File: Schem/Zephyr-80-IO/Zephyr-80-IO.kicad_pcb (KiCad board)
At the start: 6 copper layers, 160 x 64.4 mm, 89 parts, among them IC1 Z80CTC, IC2 Z80SIO, IC3 Z80SIO, J1 pBITzBus, J2 548190519, J3 L77HDA26SD1CH4F, SW1 SW_Push, SW2 SW_Push, SW3 SW_Coded_SH-7070, SW4 SW_Coded_SH-7070, SW5 SW_Coded_SH-7070, SW6 SW_Coded_SH-7070, SW7 SW_Coded_SH-7030, SW8 SW_Coded_SH-7030, U1 ATmega1284-PU, U10 74HC688, U11 74HC688, U12 74HC688, U13 74HC244, U14 MAX202IDR, U2 74AHC1G125, U3 74AHC1G125, U4 74AHC595, U5 74AHC595, U6 74HC138, U7 FT230XS-U, U8 SN74HC4040DR, U9 74HC688, Y1 ECS-2100AX-147.4

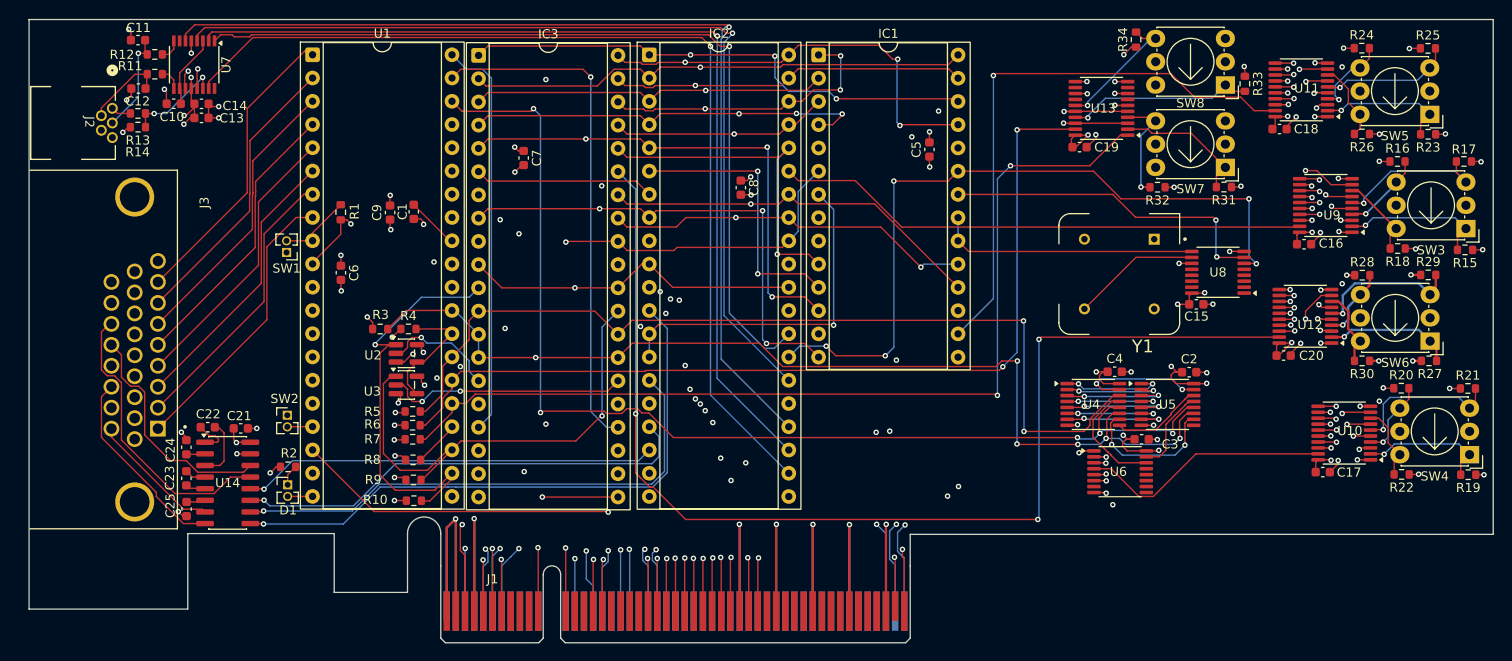
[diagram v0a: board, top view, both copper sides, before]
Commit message: Fixed a placement issue with the SMD under the socket
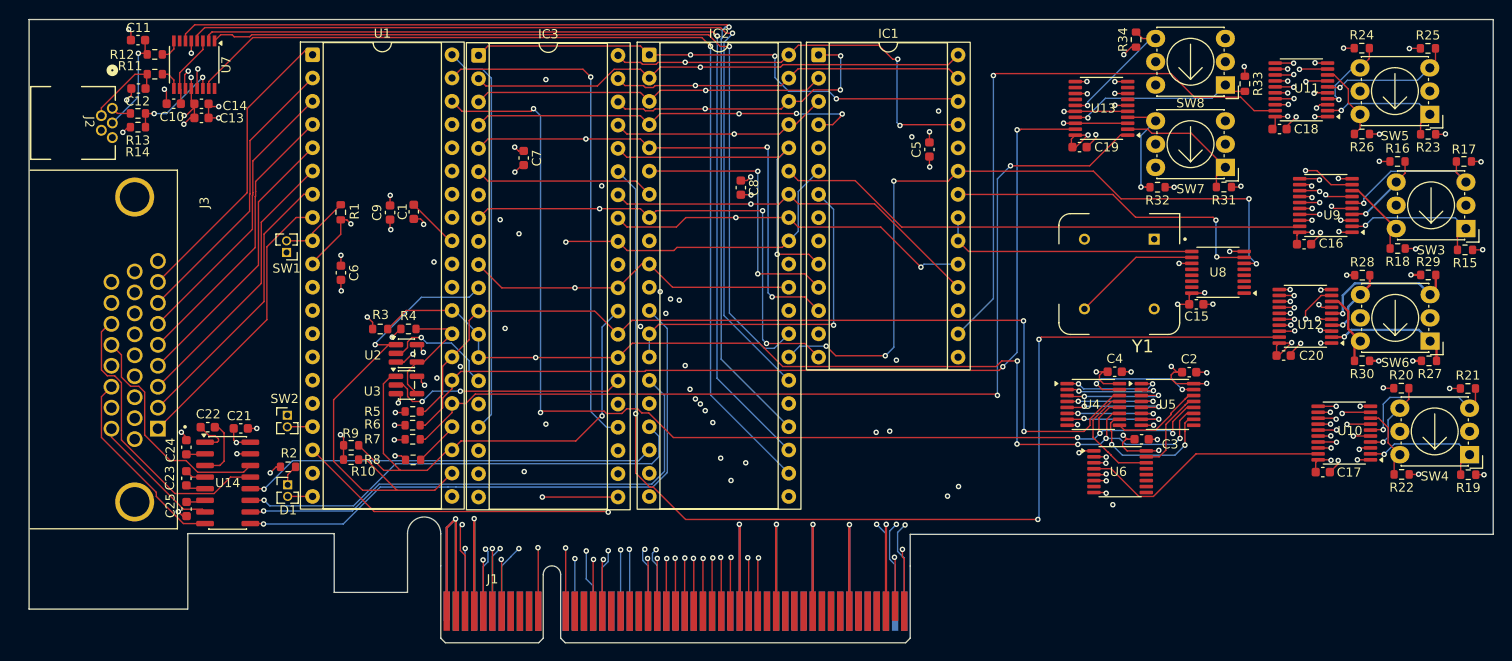
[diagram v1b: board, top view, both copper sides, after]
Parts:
- moved R10 8.20 mm to (111.7, 98.7)
- moved R9 7.78 mm to (111.7, 97.2)
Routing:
- net /IO Controller Card/~{CS_SIO_SD}: track 46.5 -> 54.1 mm
- net /IO Controller Card/~{CS_SIO_USB}: track 53.9 -> 54.8 mm
- net +5V: vias 54 -> 53
- net GND: vias 91 -> 88

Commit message: Updated the IO Controller to use the PIC18F57Q84-I/PT instead of the AVR
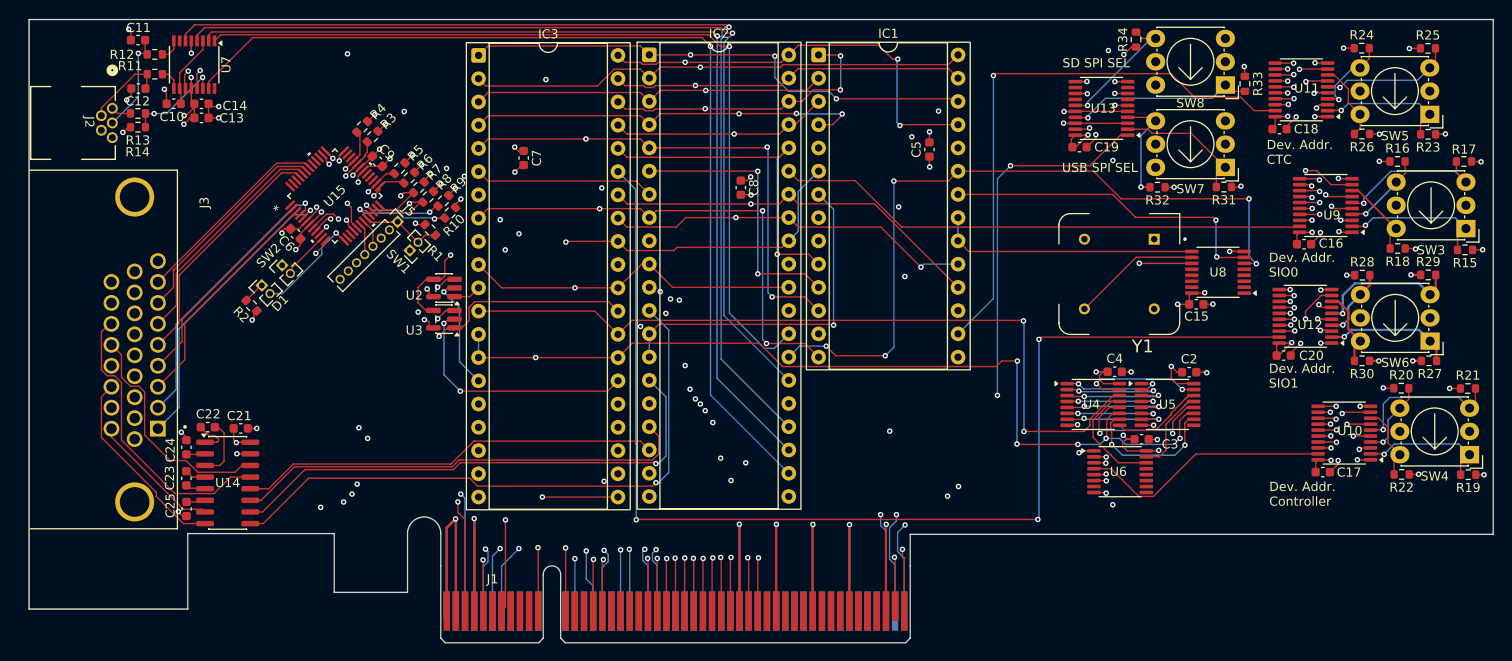
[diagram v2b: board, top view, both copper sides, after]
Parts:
- removed C1: 100n, Capacitor_SMD:C_0603_1608Metric
- removed U1: ATmega1284-PU, Package_DIP:DIP-40_W15.24mm_Socket
- added J5: Conn_01x08_Pin, Connector_PinHeader_1.27mm:PinHeader_1x08_P1.27mm_Vertical, F.Cu at (116.8, 72.7)
- added U15: PIC18F57Q84-I/PT, Footprints:TQFP48_PT_MCH, F.Cu at (110.0, 69.9)
- moved R10 29.1 mm to (122.5, 71.8), turned to -135 degrees
- moved R8 28.8 mm to (120.1, 70.0), turned to -135 degrees
- moved R9 28.6 mm to (121.8, 70.5), turned to -135 degrees
- moved R7 27.5 mm to (119.1, 69.0), turned to -135 degrees
- moved R6 27.0 mm to (118.1, 67.9), turned to -135 degrees
- moved R5 26.6 mm to (117.0, 66.9), turned to -135 degrees
- moved R4 22.7 mm to (112.9, 62.4), turned to -135 degrees
- moved D1 22.0 mm to (102.0, 79.7), turned to 45 degrees
- moved R3 21.0 mm to (114.1, 63.4), turned to -135 degrees
- moved R2 18.1 mm to (100.8, 81.9), turned to -45 degrees
- moved SW2 16.4 mm to (104.2, 77.5), turned to 45 degrees
- moved SW1 13.5 mm to (118.1, 75.9), turned to 135 degrees
- moved R1 9.97 mm to (120.4, 73.6), turned to -45 degrees
- moved U3 8.28 mm to (121.9, 83.4), turned to 180 degrees
- moved U2 8.24 mm to (121.9, 80.0), turned to 180 degrees
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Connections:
- net Net-(U1-~{RESET}) renamed /IO Controller Card/~{MCLR}
- J1 pad B6: /IO Controller Card/CLK_20M -> /pBITz Bus Interface/CLK_20M
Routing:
- net /IO Controller Card/CLK_20M: track 53.1 -> 0.00 mm, vias 2 -> 0
- net /IO Controller Card/~{USB_INT}: track 72.3 -> 107.0 mm, vias 2 -> 3
- net /IO Controller Card/MISO: track 91.9 -> 123.8 mm, vias 2 -> 5
- net /IO Controller Card/~{RESET}: track 234.2 -> 265.8 mm, vias 9 -> 10
- net /IO Controller Card/~{NMI}: track 46.2 -> 77.6 mm, vias 2 -> 4
- net /IO Controller Card/~{CS_SIO_SD}: track 54.1 -> 23.8 mm, vias 1 -> 2
- net /IO Controller Card/SD_PRESENT: track 40.2 -> 68.7 mm, vias 2 -> 3
- net /IO Controller Card/SPI_CLK: track 139.8 -> 165.9 mm, vias 7 -> 9
- net /Baud Clock/RESET_HIGH: track 110.7 -> 134.6 mm, vias 2 -> 4
- net /IO Controller Card/~{POWER_OFF}: track 40.8 -> 60.7 mm, vias 2 -> 3
- net /IO Controller Card/~{POWER_OFF_RQ}: track 43.7 -> 62.9 mm, vias 2 -> 3
- net /IO Controller Card/MOSI: track 133.8 -> 147.0 mm, vias 4 -> 6
- net /GPIOs and User Serial/GPIO7: track 32.9 -> 22.1 mm
- net /IO Controller Card/CTRL_LAT: track 123.0 -> 133.4 mm, vias 5 -> 4
- net /IO Controller Card/~{SIO1B_INT}: track 56.2 -> 66.3 mm, vias 1 -> 2
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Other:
- board text added: "Dev. Addr. CTC"
- board text added: "Dev. Addr. Controller"
- board text added: "Dev. Addr. SIO0"
- board text added: "Dev. Addr. SIO1"
- board text added: "SD SPI SEL"
- board text added: "USB SPI SEL"

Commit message: synching
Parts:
- added G***: LOGO, Footprints:pBITzlogo-Silk, F.Cu at (111.6, 93.3)
- added REF**: OSHW-Logo2_7.3x6mm_SilkScreen, Symbol:OSHW-Logo2_7.3x6mm_SilkScreen, F.Cu at (119.9, 98.1)
- moved J2 1.28 mm to (84.3, 60.3)
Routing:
- net /Console Port/DM1: track 9.00 -> 10.5 mm
- net /Console Port/VBUS_PIN1: track 2.21 -> 3.50 mm
- net /Console Port/DP1: track 11.5 -> 12.7 mm
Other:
- board text added: "MULTIPUPOSE USER PORT"
- board text added: "NMI_RQ"
- board text added: "RESET"
- board text added: "SD BUSY"

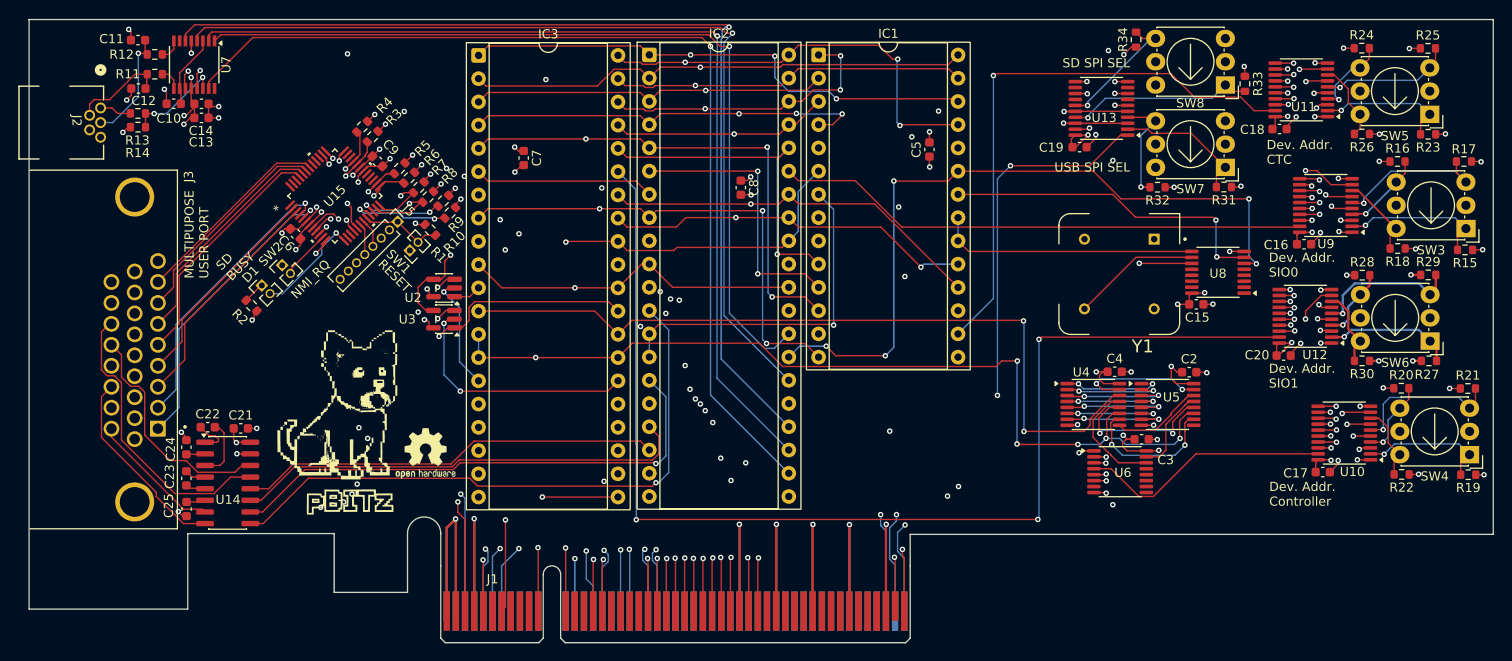
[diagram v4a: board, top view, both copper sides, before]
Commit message: Added copper pours on top and bottom layers of IO controller board, and added a few vias to connect them. This should help with heat dissipation and EMI shielding.
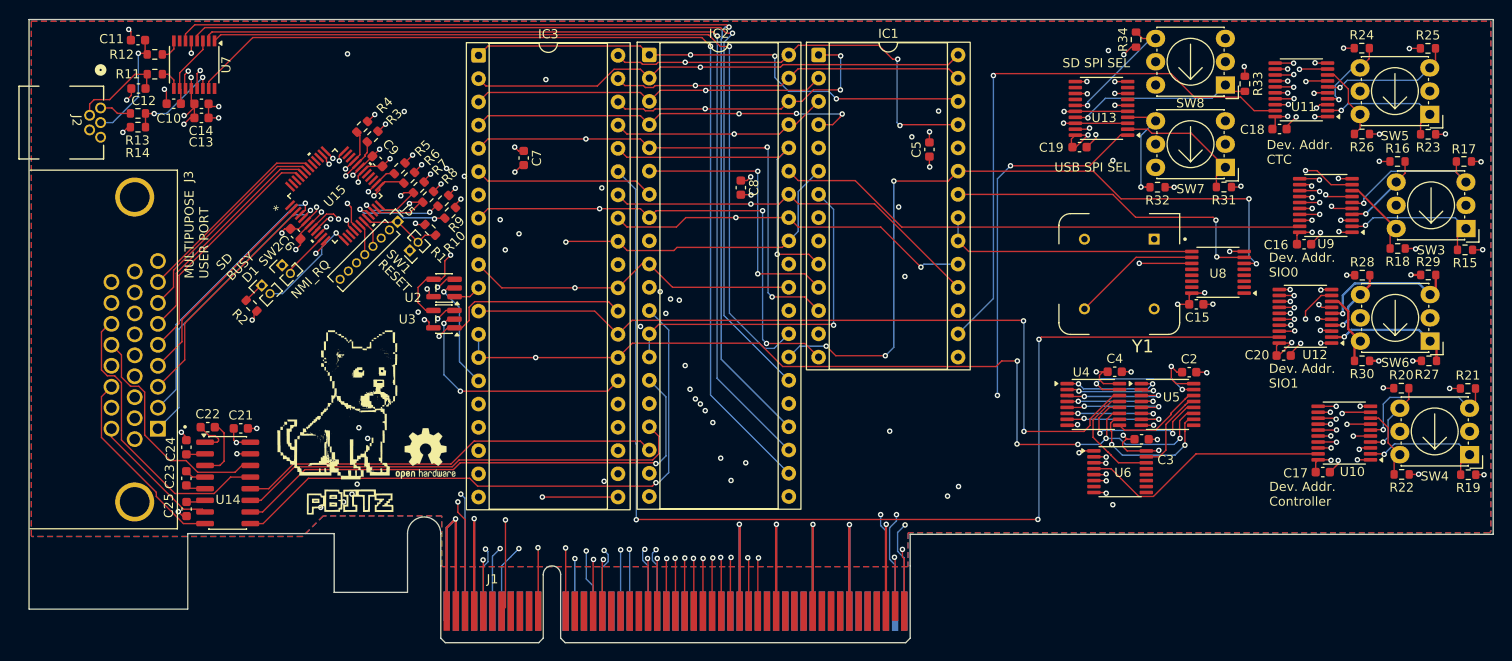
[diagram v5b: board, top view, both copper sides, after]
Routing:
- added copper zone on B.Cu, net GND
- added copper zone on F.Cu, net GND
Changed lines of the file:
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@@
+		(net 1)
+		(net_name "GND")
+		(layers "F.Cu" "B.Cu")
+		(hatch edge 0.5)
+		(priority 3)
+		(connect_pads no
+			(clearance 0.4)
+		)
+		(min_thickness 0.127)
+		(filled_areas_thickness no)
+		(fill yes
+			(thermal_gap 0.254)
+			(thermal_bridge_width 0.3254)
+			(smoothing chamfer)
+		)
+		(polygon
+			(pts
+				(xy 76.78 50.84) (xy 236.28 50.84) (xy 236.28 106.59) (xy 236.13 106.74) (xy 172.58 106.74) (xy 172.58 110.39)
+				(xy 172.53 110.44) (xy 121.73 110.44) (xy 121.63 110.34) (xy 121.63 104.89) (xy 108.68 104.89) (xy 106.43 107.14)
+				(xy 76.83 107.14) (xy 76.78 107.09)
+			)
+		)
+	)
+	(zone
 		(net 1)
 		(net_name "GND")
